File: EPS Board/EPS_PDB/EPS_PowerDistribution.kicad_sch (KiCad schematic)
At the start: 73 parts, among them U10 TPS259621DDAT, U11 LTC3624IDD-25PBF, U12 TPS259621DDAT, U13 TPS259621DDAT, U14 TPS259621DDAT, U15 TPS259621DDAT, U16 TPS259621DDAT, U17 LM5000-3MTCX, U18 AD7708BRUZ, U2 TS4061BICT-1.25, U6 TPS259621DDAT, U7 TPS259621DDAT, U9 TPS259621DDAT, Y4 32.768kHz

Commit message: Footprint assignment on EPS PDB Board
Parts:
- 120R2: renamed from 120R3; footprint (none) -> Resistor_SMD:R_0805_2012Metric
- C17: renamed from C29; footprint (none) -> Capacitor_SMD:C_0805_2012Metric
- C18: renamed from C30; footprint (none) -> Capacitor_SMD:C_0805_2012Metric
- C25: renamed from C33; footprint (none) -> Capacitor_SMD:C_0805_2012Metric
- C26: renamed from C34; footprint (none) -> Capacitor_SMD:C_0805_2012Metric
- C27: renamed from C35; footprint (none) -> Capacitor_SMD:C_0805_2012Metric
- C28: renamed from C36; footprint (none) -> Capacitor_SMD:C_0805_2012Metric
- C29: renamed from C37; footprint (none) -> Capacitor_SMD:C_0805_2012Metric
- C31: renamed from C32; footprint (none) -> Capacitor_SMD:C_0805_2012Metric
- C32: renamed from C31; footprint (none) -> Capacitor_SMD:C_0805_2012Metric
- D3: renamed from D4; footprint (none) -> Diode_SMD:D_0805_2012Metric
- D4: renamed from D3; footprint (none) -> Diode_SMD:D_0805_2012Metric
- JP3: footprint (none) -> Jumper:SolderJumper-3_P1.3mm_Open_RoundedPad1.0x1.5mm
- JP4: renamed from JP5; footprint (none) -> Jumper:SolderJumper-3_P1.3mm_Open_RoundedPad1.0x1.5mm
- JP5: renamed from JP2; footprint (none) -> Jumper:SolderJumper-3_P1.3mm_Open_RoundedPad1.0x1.5mm
- R18: renamed from R23; footprint (none) -> Resistor_SMD:R_0805_2012Metric
- U10: renamed from U14; footprint EPS_Schematic_v2:IC_TPS259621DDAT -> TPS259621DDAT:IC_TPS259621DDAT
- U11: renamed from U17; footprint LM5000-3MTCX:SOP65P640X120-16N -> LM500:SOP65P640X120-16N
- U12: renamed from U6; footprint EPS_Schematic_v2:IC_TPS259621DDAT -> TPS259621DDAT:IC_TPS259621DDAT
- U13: renamed from U7; footprint EPS_Schematic_v2:IC_TPS259621DDAT -> TPS259621DDAT:IC_TPS259621DDAT
- U15: renamed from U9; footprint EPS_Schematic_v2:IC_TPS259621DDAT -> TPS259621DDAT:IC_TPS259621DDAT
- U16: renamed from U10; footprint EPS_Schematic_v2:IC_TPS259621DDAT -> TPS259621DDAT:IC_TPS259621DDAT
- U17: renamed from U8; value ~ -> LTC3624EMSE-3.3PBF; footprint EPS_Schematic_v2:SOP65P490X110-13N -> LTC3624EMSE-3.3PBF:SOP65P490X110-13N
- U18: renamed from U12; footprint EPS_Schematic_v2:IC_TPS259621DDAT -> TPS259621DDAT:IC_TPS259621DDAT
- U19: renamed from U11; footprint (none) -> LTC3624IDD-25PBF:DFN-8_DD
- U6: renamed from U2; footprint SOT323-3L_1P35X2P2X0P65_STM -> TS4061BICT:SOT323-3L_1P35X2P2X0P65_STM
- U7: renamed from U15; footprint EPS_Schematic_v2:IC_TPS259621DDAT -> TPS259621DDAT:IC_TPS259621DDAT
- U8: renamed from U16; footprint EPS_Schematic_v2:IC_TPS259621DDAT -> TPS259621DDAT:IC_TPS259621DDAT
- U9: renamed from U13; footprint EPS_Schematic_v2:IC_TPS259621DDAT -> TPS259621DDAT:IC_TPS259621DDAT
- Y2: renamed from Y4; footprint (none) -> Crystal:Crystal_SMD_3215-2Pin_3.2x1.5mm
- renumbered C26 to C19, C23 to C20, C24 to C21, C25 to C22, C27 to C23, C28 to C24, C18 to C30, C17 to C33, C19 to C34, C20 to C35, C21 to C36, C22 to C37, L3 to L1, L1 to L2, L2 to L3, R24 to R13, R25 to R14, R26 to R15, R27 to R16, R28 to R17, R37 to R19, R38 to R20, R30 to R21, R31 to R22, R39 to R23, R40 to R24, R34 to R25, R32 to R26, R22 to R27, R29 to R28, R35 to R29, R33 to R30, R36 to R31, R13 to R32, R15 to R33, R14 to R34, R16 to R35, R17 to R36, R19 to R37, R18 to R38, R20 to R39, R21 to R40, U18 to U14
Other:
- note added: "SOMETHING WRONG HERE"

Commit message: PDB PCB Design Progress
Board outline copy pasted from Antenna Deployment Board
Added current limiter datasheet
Routed USB differential pair
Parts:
- U10: value TPS259621DDAT -> TPS259621DDAT_5V_PAY
- U12: value TPS259621DDAT -> TPS259621DDAT_5V_EPS
- U13: value TPS259621DDAT -> TPS259621DDAT_5V_OBC
- U15: value TPS259621DDAT -> TPS259621DDAT_5V_ADCS
- U16: value TPS259621DDAT -> TPS259621DDAT_5V_COMM
- U18: value TPS259621DDAT -> TPS259621DDAT_12V_ADCS
- U7: value TPS259621DDAT -> TPS259621DDAT 3V3_ADCS
- U8: value TPS259621DDAT -> TPS259621DDAT_3V3_ANT
- U9: value TPS259621DDAT -> TPS259621DDAT_3V3_EPS
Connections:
- net 12V: now reaches R29.2, R31.2, U11.2 (FB)
- net VIN: now reaches C19.2, R25.1, U11.13 (VIN)
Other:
- moved on the sheet: R25
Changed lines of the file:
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@@
 	(wire
 		(pts
+			(xy 245.11 127) (xy 245.11 136.525)
+		)
+		(stroke
+			(width 0)
+			(type default)
+		)
+	)
+	(wire
+		(pts
 			(xy 101.6 193.04) (xy 101.6 193.675)
 		)
@@
 	(wire
 		(pts
+			(xy 219.71 127) (xy 226.695 127)
+		)
+		(stroke
+			(width 0)
+			(type default)
+		)
+	)
+	(wire
+		(pts
 			(xy 240.03 83.82) (xy 240.03 88.9)
 		)
@@
 	(wire
 		(pts
+			(xy 236.855 127) (xy 245.11 127)
+		)
+		(stroke
+			(width 0)
+			(type default)
+		)
+	)
+	(wire
+		(pts
 			(xy 342.9 240.03) (xy 346.075 240.03)
 		)
@@
 	(wire
 		(pts
-			(xy 240.03 126.365) (xy 245.11 126.365)
-		)
-		(stroke
-			(width 0)
-			(type default)
-		)
-	)
-	(wire
-		(pts
 			(xy 101.6 234.315) (xy 97.79 234.315)
 		)
@@
 	(text "12V REGULATOR"
 		(exclude_from_sim no)
-		(at 215.9 127 0)
+		(at 267.335 126.365 0)
 		(effects
 			(font
@@
 		)
 	)
+	(label "VIN"
+		(at 245.11 131.445 0)
+		(fields_autoplaced yes)
+		(effects
+			(font
+				(size 1.27 1.27)
+			)
+			(justify left bottom)
+		)
+	)
 	(label "ILM_3V3_ANT"
 		(at 342.9 224.79 180)
@@
 		)
 	)
+	(label "12V"
+		(at 243.84 151.765 0)
+		(fields_autoplaced yes)
+		(effects
+			(font
+				(size 1.27 1.27)
+			)
+			(justify left bottom)
+		)
+	)
 	(label "5V_BUS"
 		(at 55.88 173.355 180)
@@
 	(hierarchical_label "VBUS"
 		(shape input)
-		(at 240.03 126.365 180)
+		(at 219.71 127 180)
 		(fields_autoplaced yes)
 		(effects
@@
 			)
 		)
-		(property "Value" "TPS259621DDAT"
+		(property "Value" "TPS259621DDAT_5V_OBC"
 			(at 133.35 198.755 0)
 			(effects
@@
 			)
 		)
-		(property "Value" "TPS259621DDAT"
+		(property "Value" "TPS259621DDAT_5V_ADCS"
 			(at 64.77 239.395 0)
 			(effects
@@
 			)
 		)
-		(property "Value" "TPS259621DDAT"
+		(property "Value" "TPS259621DDAT 3V3_ADCS"
 			(at 64.77 114.935 0)
 			(effects
@@
 			)
 		)
-		(property "Value" "TPS259621DDAT"
+		(property "Value" "TPS259621DDAT_12V_ADCS"
 			(at 63.5 278.765 0)
 			(effects
@@
 			)
 		)
-		(property "Value" "TPS259621DDAT"
+		(property "Value" "TPS259621DDAT_3V3_EPS"
 			(at 64.77 156.845 0)
 			(effects
@@
 	(symbol
 		(lib_id "EPS_Schematic_v2-eagle-import:R-USCHIP-0805(2012-METRIC)")
-		(at 245.11 131.445 90)
+		(at 231.775 127 180)
 		(unit 1)
 		(exclude_from_sim no)
@@
 		(dnp no)
 		(property "Reference" "R25"
-			(at 242.3414 131.445 0)
+			(at 231.775 129.7686 0)
 			(effects
 				(font
@@
 		)
 		(property "Value" "10"
-			(at 248.412 131.445 0)
+			(at 229.87 124.46 0)
 			(effects
 				(font
@@
 		)
 		(property "Footprint" "Resistor_SMD:R_0603_1608Metric_Pad0.98x0.95mm_HandSolder"
-			(at 245.11 131.445 0)
+			(at 231.775 127 0)
 			(effects
 				(font
@@
 		)
 		(property "Datasheet" ""
-			(at 245.11 131.445 0)
+			(at 231.775 127 0)
 			(effects
 				(font
@@
 		)
 		(property "Description" ""
-			(at 245.11 131.445 0)
+			(at 231.775 127 0)
 			(effects
 				(font
@@
 			)
 		)
-		(property "Value" "TPS259621DDAT"
+		(property "Value" "TPS259621DDAT_5V_EPS"
 			(at 64.77 198.755 0)
 			(effects
@@
 			)
 		)
-		(property "Value" "TPS259621DDAT"
+		(property "Value" "TPS259621DDAT_5V_PAY"
 			(at 133.35 156.845 0)
 			(effects
@@
 			)
 		)
-		(property "Value" "TPS259621DDAT"
+		(property "Value" "TPS259621DDAT_5V_COMM"
 			(at 133.35 239.395 0)
 			(effects
@@
 			)
 		)
-		(property "Value" "TPS259621DDAT"
+		(property "Value" "TPS259621DDAT_3V3_ANT"
 			(at 133.35 114.935 0)
 			(effects

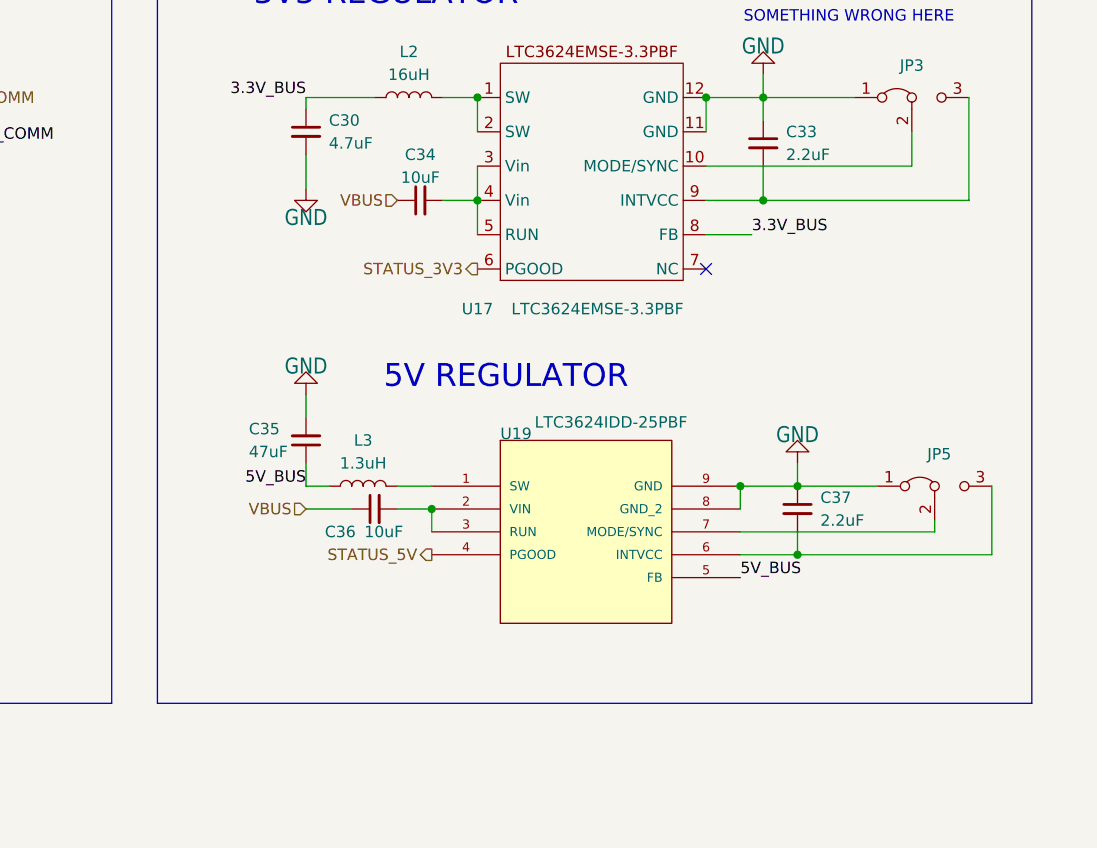
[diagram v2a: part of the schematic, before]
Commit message: EPS PDB Board Layout Progress
Fixed issue with outline,
added correct outline
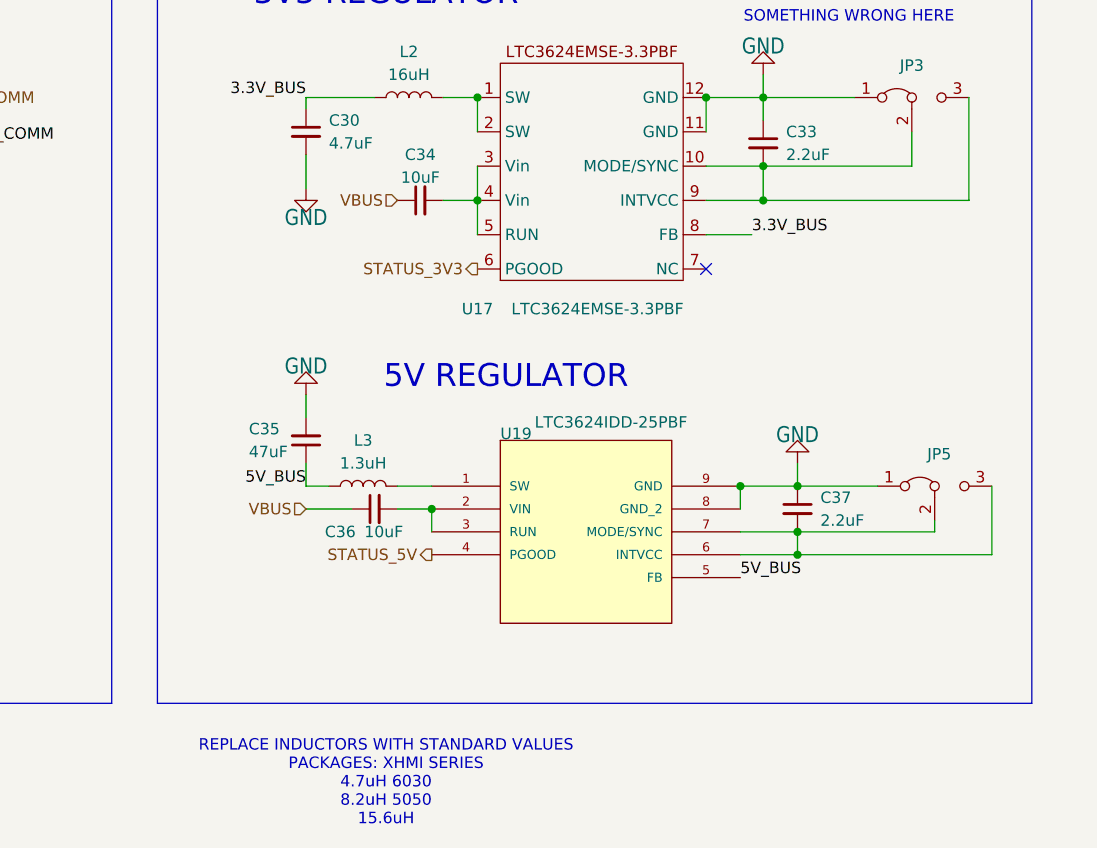
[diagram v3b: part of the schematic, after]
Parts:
- C17, C18, C25, C26, C27, C28, C29, C31, C32: footprint Capacitor_SMD:C_0805_2012Metric -> Capacitor_SMD:C_0603_1608Metric
- C19, C20, C21, C22, C23, C24, C30, C33, C34, C35, C36, C37: footprint Capacitor_SMD:C_0805_2012Metric_Pad1.18x1.45mm_HandSolder -> Capacitor_SMD:C_0603_1608Metric
- R13, R14, R15, R16, R17, R19, R20, R21, R22, R23, R24, R25, R26, R27, R28, R29, R30, R31, R32, R33, R34, R35, R36, R37, R38, R39, R40: footprint Resistor_SMD:R_0603_1608Metric_Pad0.98x0.95mm_HandSolder -> Resistor_SMD:R_0603_1608Metric
- R18: footprint Resistor_SMD:R_0805_2012Metric -> Resistor_SMD:R_0603_1608Metric
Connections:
- net at C37.2, JP5.3 (B), U19.6 (INTVCC): now also JP5.2 (C), U19.7 (MODE/SYNC)
- net at C33.2, JP3.3 (B), U17.9 (INTVCC): now also JP3.2 (C), U17.10 (MODE/SYNC)
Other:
- note added: "REPLACE INDUCTORS WITH STANDARD VALUES PACKAGES: XHMI SERIES 4.7uH 6030 8.2uH 5050 15.6uH"

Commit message: EPS PDB Layout
Power Distribution and Regulation unit layout started
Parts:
- L1, L2: footprint Inductor_SMD:L_0805_2012Metric_Pad1.15x1.40mm_HandSolder -> Inductor_SMD:L_Wuerth_WE-XHMI-8080
- L3: footprint Inductor_SMD:L_0805_2012Metric_Pad1.15x1.40mm_HandSolder -> Inductor_SMD:L_1206_3216Metric
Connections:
- net at C33.2, JP3.3 (B), U17.9 (INTVCC): no longer JP3.2 (C), U17.10 (MODE/SYNC)
- new net MODE: JP3.2 (C), U17.10 (MODE/SYNC)
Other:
- note added: "For fixed VOUT options, connect FB pin directly to VOUT."
- note added: "IRMS = IOUT(Max)*(0.497) IOUT(Max) = 1A"
- note added: "Input Capacitor (CIN) Selection The input capacitance, CIN, is needed to filter the square wave current at the drain of the top power MOSFET. To prevent large voltage transients from occurring, a low ESR input capacitor sized for the maximum RMS current should be used. The maximum RMS current is given by:"
- note added: "L = (3.3/2.25*0.4)(1-(3.3/7.4)) L = 2.0314 uH"
- note added: "VIN = 7.4 V VOUT = 3.3 V IOUT (Max) = 2A IOUT (Min) = 0A f = 2.25 MHz"
- note removed: "SOMETHING WRONG HERE"
- moved on the sheet: 120R2, C17, C18, C25, C26, C27, C28, C29, C30, C31, C32, C33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
